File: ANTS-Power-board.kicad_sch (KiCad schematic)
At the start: 8 parts, among them J1 DF11-12DP, J2 DF11-12DP, J3 Phoenix 1751248, J4 Phoenix 1751248

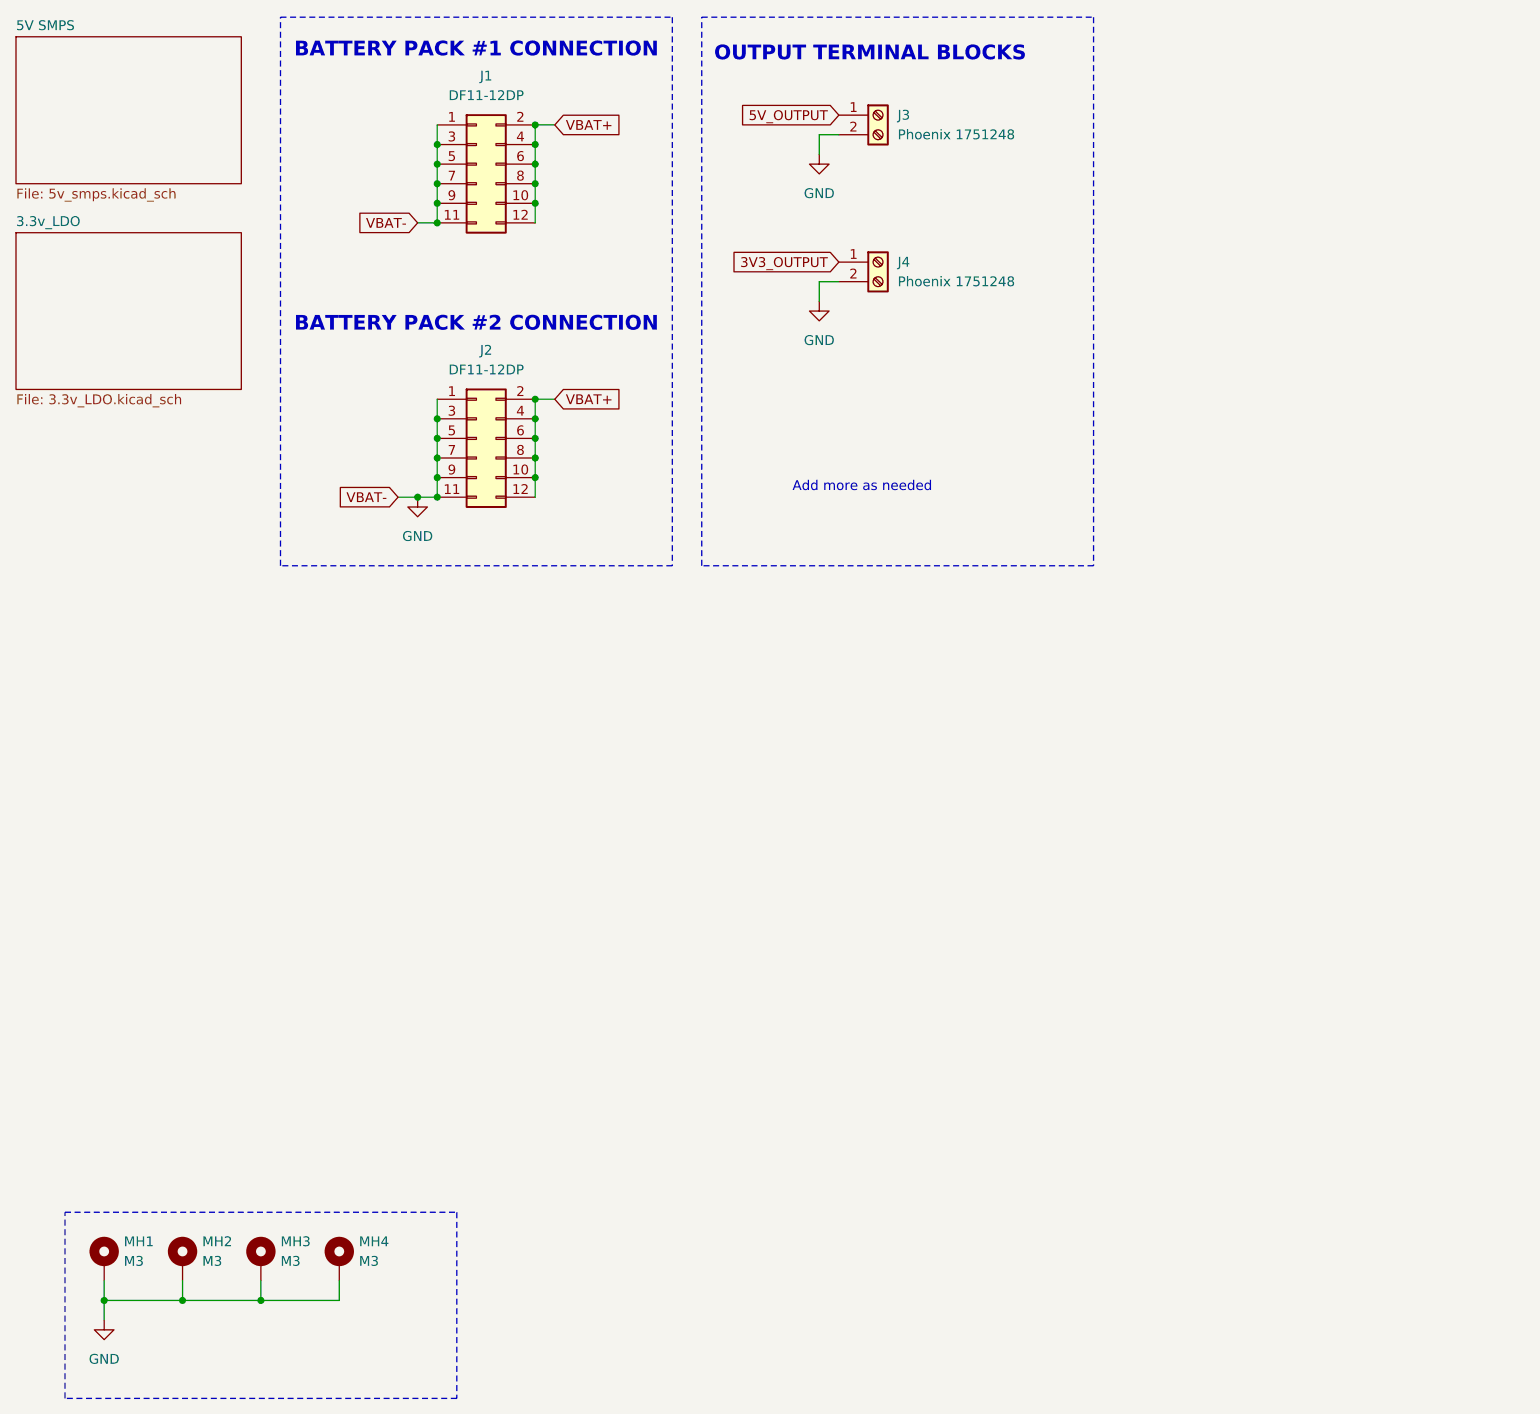
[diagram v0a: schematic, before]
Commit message: schematic for new DF11 and WJ127 connectors
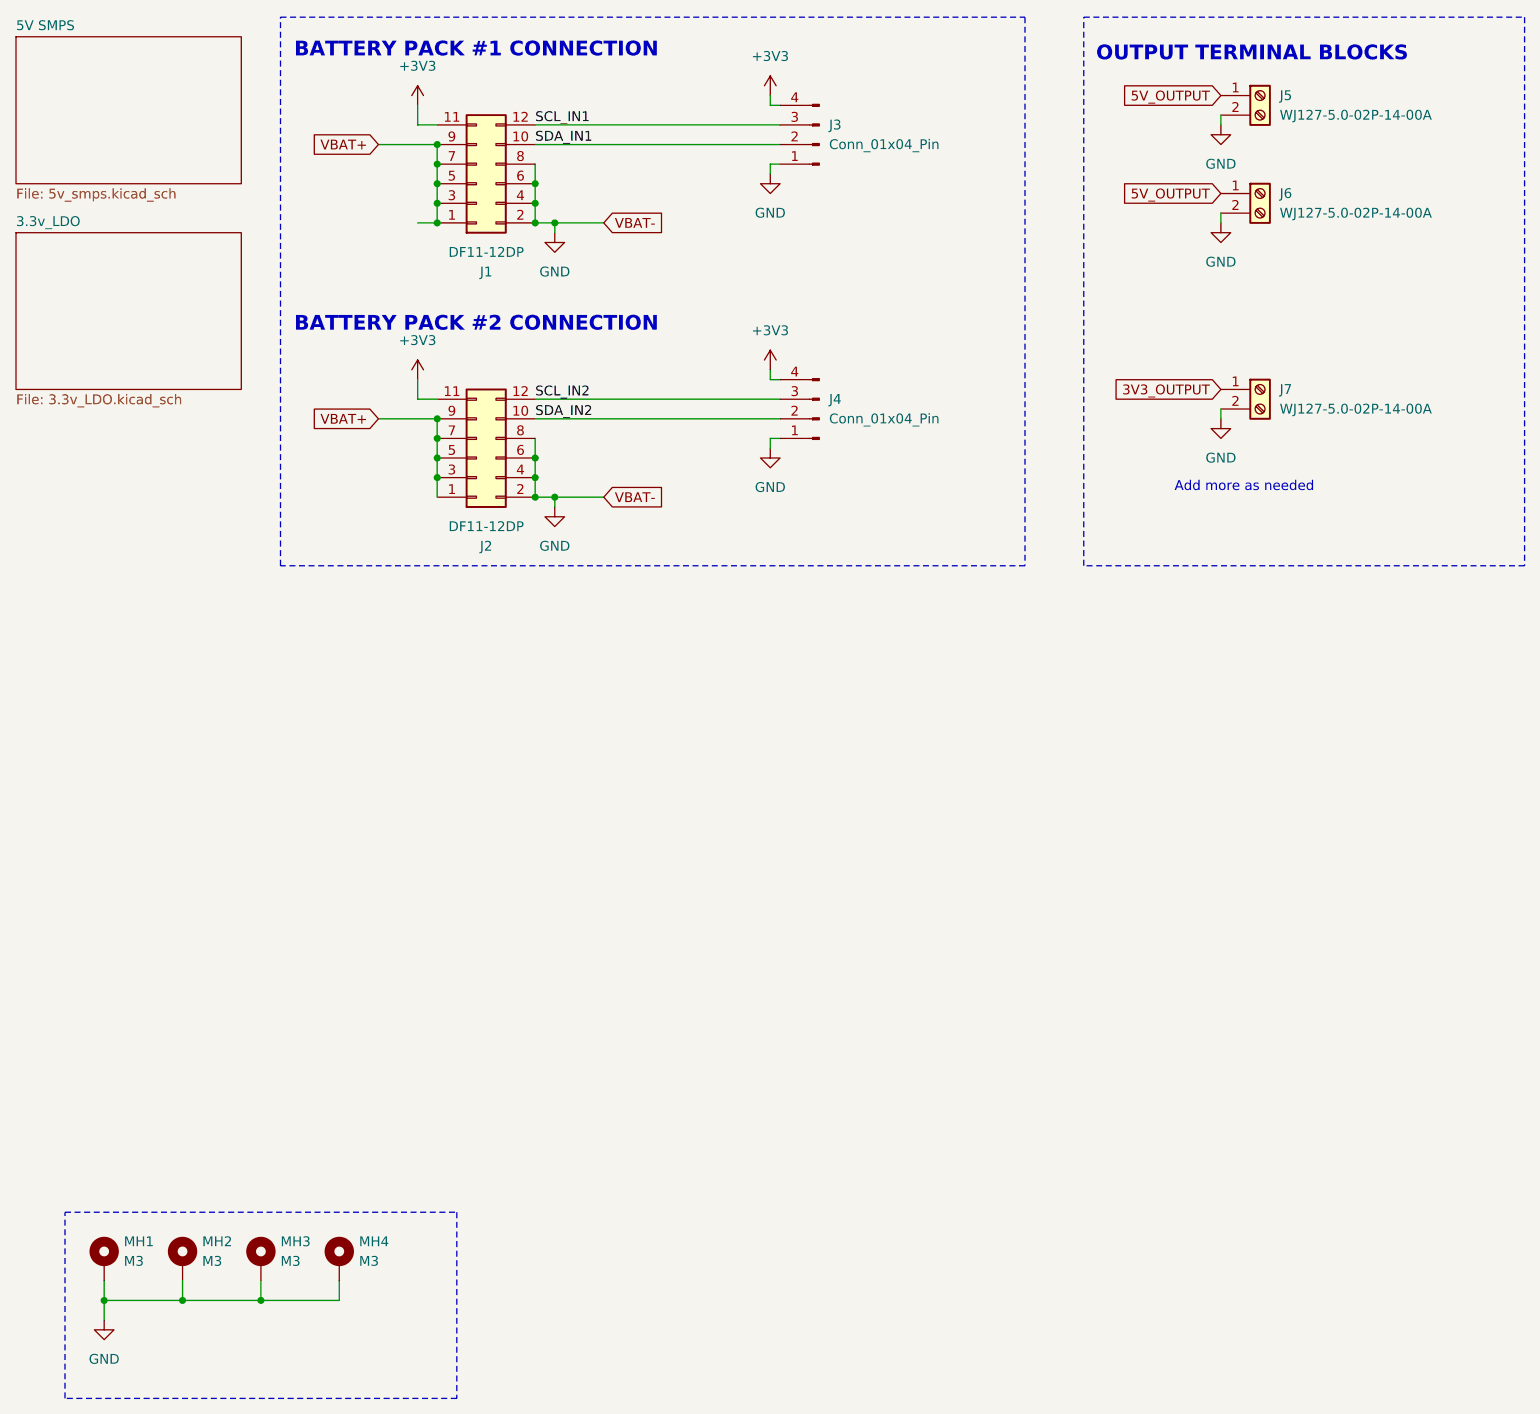
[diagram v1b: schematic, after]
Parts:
- added J3, J4: Conn_01x04_Pin, Connector_PinSocket_2.54mm:PinSocket_1x04_P2.54mm_Vertical, symbol Connector:Conn_01x04_Pin
- added J6: WJ127-5.0-02P-14-00A, ScrewTerminal:CONN-TH_MKDS1-2-3.5, symbol Connector:Screw_Terminal_01x02
- J5: renamed from J3; value Phoenix 1751248 -> WJ127-5.0-02P-14-00A; LCSC C89122 -> (none); now left out of the parts list
- J7: renamed from J4; value Phoenix 1751248 -> WJ127-5.0-02P-14-00A; LCSC C89122 -> (none); now left out of the parts list
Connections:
- net 5V_OUTPUT: now also J6.1 (Pin_1)
- net GND: now also J1.2 (Pin_2), J1.4 (Pin_4), J1.6 (Pin_6), J1.8 (Pin_8), J2.2 (Pin_2), J2.4 (Pin_4), J2.6 (Pin_6), J2.8 (Pin_8), J3.1 (Pin_1), J4.1 (Pin_1), J6.2 (Pin_2); no longer J1.1 (Pin_1), J1.11 (Pin_11), J1.3 (Pin_3), J1.5 (Pin_5), J1.7 (Pin_7), J1.9 (Pin_9), J2.1 (Pin_1), J2.11 (Pin_11), J2.3 (Pin_3), J2.5 (Pin_5), J2.7 (Pin_7), J2.9 (Pin_9)
- net VBAT+: now also J1.1 (Pin_1), J1.3 (Pin_3), J1.5 (Pin_5), J1.7 (Pin_7), J1.9 (Pin_9), J2.1 (Pin_1), J2.3 (Pin_3), J2.5 (Pin_5), J2.7 (Pin_7), J2.9 (Pin_9); no longer J1.10 (Pin_10), J1.12 (Pin_12), J1.2 (Pin_2), J1.4 (Pin_4), J1.6 (Pin_6), J1.8 (Pin_8), J2.10 (Pin_10), J2.12 (Pin_12), J2.2 (Pin_2), J2.4 (Pin_4), J2.6 (Pin_6), J2.8 (Pin_8)
- new net +3V3: J1.11 (Pin_11), J2.11 (Pin_11), J3.4 (Pin_4), J4.4 (Pin_4)
- new net SCL_IN1: J1.12 (Pin_12), J3.3 (Pin_3)
- new net SCL_IN2: J2.12 (Pin_12), J4.3 (Pin_3)
- new net SDA_IN1: J1.10 (Pin_10), J3.2 (Pin_2)
- new net SDA_IN2: J2.10 (Pin_10), J4.2 (Pin_2)
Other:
- moved on the sheet: J5, J7

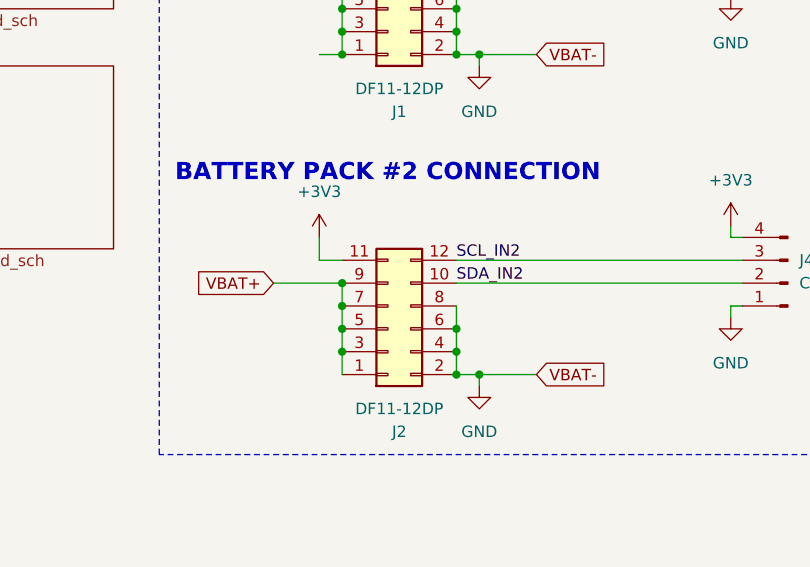
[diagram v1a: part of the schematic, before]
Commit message: update to batt pack v2 (red). add screw terminal
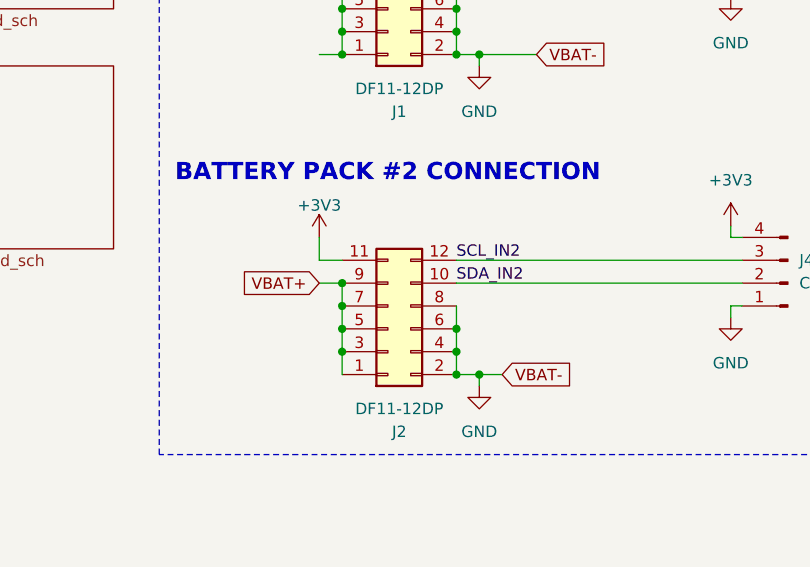
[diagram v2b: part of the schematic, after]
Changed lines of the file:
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@@
 	(wire
 		(pts
-			(xy 86.36 77.47) (xy 92.71 77.47)
+			(xy 86.36 77.47) (xy 88.9 77.47)
 		)
 		(stroke
@@
 	(wire
 		(pts
-			(xy 63.5 67.31) (xy 71.12 67.31)
+			(xy 68.58 67.31) (xy 71.12 67.31)
 		)
 		(stroke
@@
 	(global_label "VBAT+"
 		(shape input)
-		(at 63.5 67.31 180)
+		(at 68.58 67.31 180)
 		(fields_autoplaced yes)
 		(effects
@@
 		)
 		(property "Intersheetrefs" "${INTERSHEET_REFS}"
-			(at 54.5276 67.31 0)
+			(at 59.6076 67.31 0)
 			(effects
 				(font
@@
 	(global_label "VBAT-"
 		(shape input)
-		(at 92.71 77.47 0)
+		(at 88.9 77.47 0)
 		(fields_autoplaced yes)
 		(effects
@@
 		)
 		(property "Intersheetrefs" "${INTERSHEET_REFS}"
-			(at 101.6824 77.47 0)
+			(at 97.8724 77.47 0)
 			(effects
 				(font
@@
 		(on_board yes)
 		(dnp no)
-		(fields_autoplaced yes)
 		(property "Reference" "#PWR03"
 			(at 68.58 66.04 0)
@@
 		)
 		(property "Value" "+3V3"
-			(at 68.58 57.15 0)
-			(effects
-				(font
+			(at 68.58 58.674 0)
+			(effects
+				(font

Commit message: Add decorations
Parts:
- J5, J6, J7: now in the parts list
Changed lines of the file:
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@@
 		(unit 1)
 		(exclude_from_sim no)
-		(in_bom no)
+		(in_bom yes)
 		(on_board yes)
 		(dnp no)
@@
 		(unit 1)
 		(exclude_from_sim no)
-		(in_bom no)
+		(in_bom yes)
 		(on_board yes)
 		(dnp no)
@@
 		(unit 1)
 		(exclude_from_sim no)
-		(in_bom no)
-		(on_board yes)
-		(dnp no)
+		(in_bom yes)
+		(on_board yes)
+		(dnp no)
